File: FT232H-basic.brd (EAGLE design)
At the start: 57.1 x 25.4 mm, 26 parts, among them IC1 FT232H

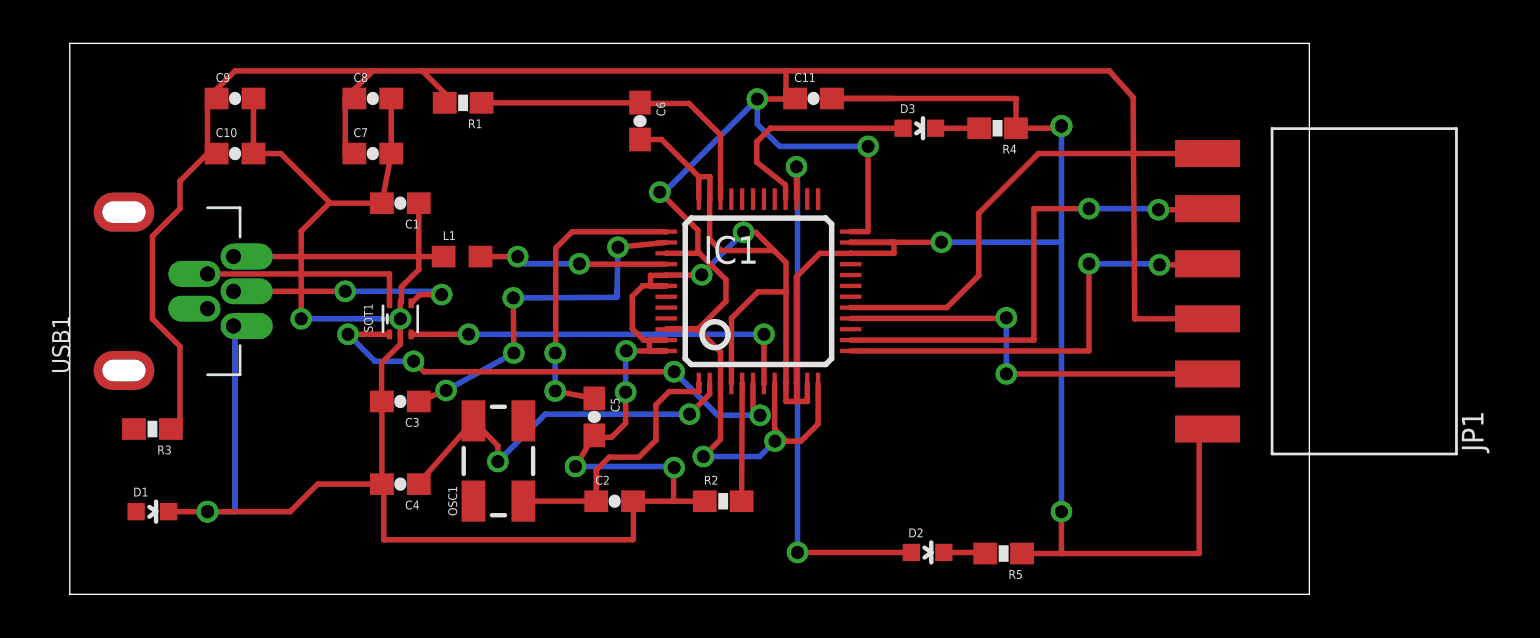
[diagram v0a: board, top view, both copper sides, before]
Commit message: routing improvements - much simpler, has bottom ground plane and top copper pour
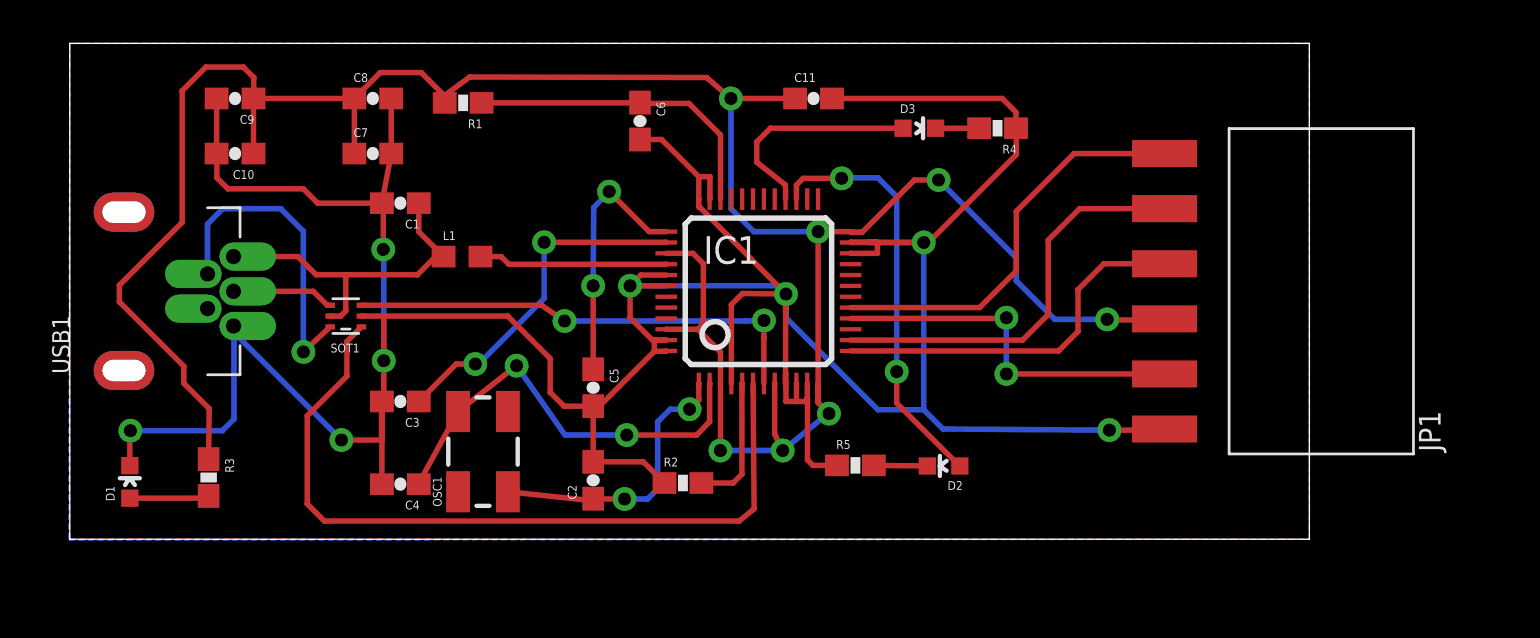
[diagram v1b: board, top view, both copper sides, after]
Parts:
- moved R5 7.95 mm to (36.2, 5.94), turned to 0 degrees
- moved D2 4.06 mm to (40.3, 5.92), turned to 90 degrees
- moved R3 3.42 mm to (6.40, 5.38), turned to 270 degrees
- moved SOT1 2.52 mm to (12.7, 12.8), turned to 90 degrees
- moved R2 2.03 mm to (28.3, 5.13)
- moved JP1 1.98 mm to (53.9, 14.0)
- moved D1 1.72 mm to (2.77, 5.18), turned to 0 degrees
- moved C2 1.38 mm to (24.1, 5.26), turned to 90 degrees
- moved C5 1.35 mm to (24.1, 9.53)
- moved OSC1 0.83 mm to (19.1, 6.58)
- turned C10 to 180 degrees
- turned C9 to 180 degrees
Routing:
- net GND: track 200.3 -> 178.4 mm, vias 12 -> 8
- net POWER: track 133.5 -> 118.5 mm, vias 5 -> 7
- net DM: track 24.1 -> 36.1 mm, vias 4 -> 0
- net N$6: track 11.2 -> 4.72 mm, vias 2 -> 0
- net RXLED: track 24.6 -> 19.4 mm
- net N$8: track 9.74 -> 14.7 mm, vias 0 -> 1
- net N$5: track 0.00 -> 3.67 mm
- net RXI: track 22.6 -> 19.0 mm, vias 2 -> 0
- net TXO: track 20.6 -> 17.3 mm, vias 2 -> 0
- net DP: track 18.5 -> 21.7 mm
- net N$7: track 17.7 -> 19.9 mm
- net N$1: track 13.9 -> 11.9 mm
- net CTS: track 19.1 -> 17.1 mm
- net DTR: track 20.7 -> 19.0 mm
- net OSC1: track 12.4 -> 13.6 mm, vias 0 -> 2
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- added copper zone on layer 16, net GND
- added copper zone on layer 1, net N$9
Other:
- board size 57.1 x 25.4 mm -> 57.1 x 22.9 mm

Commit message: board is slightly smaller now; traces in ground plane shorter
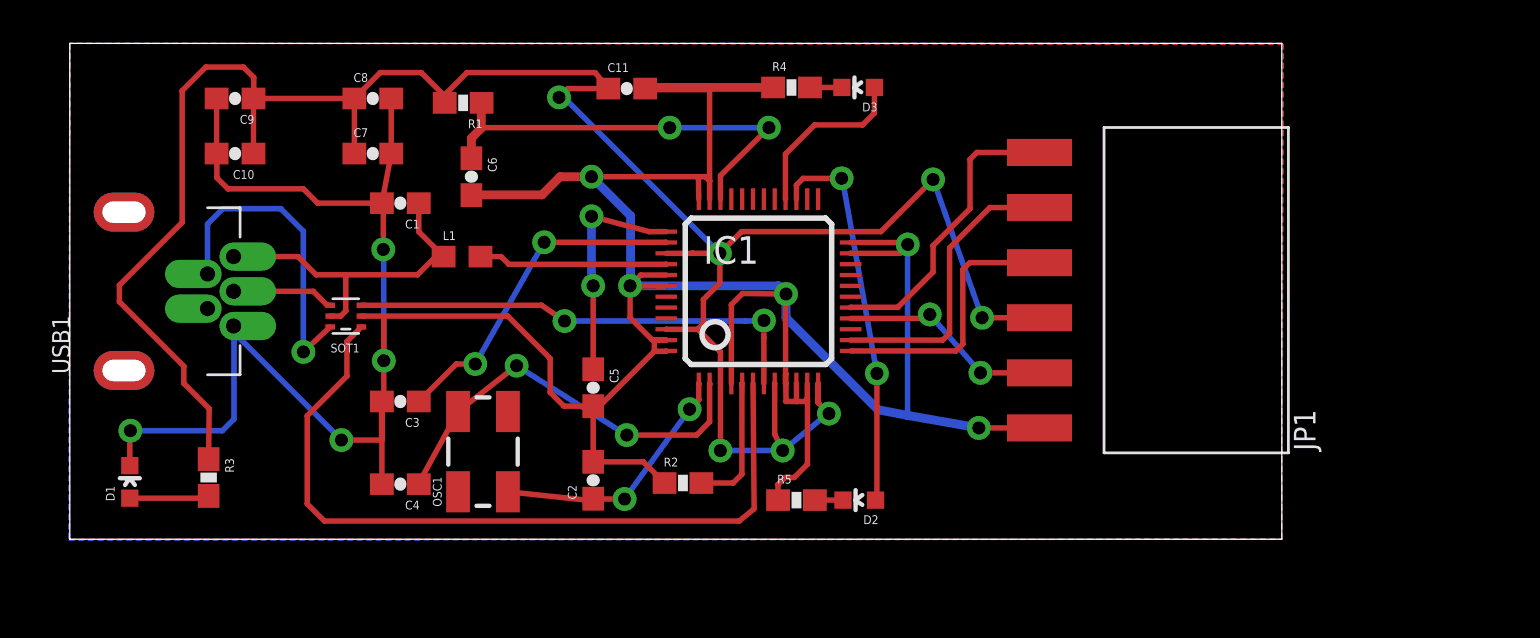
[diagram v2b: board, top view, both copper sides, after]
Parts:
- moved R4 9.68 mm to (33.3, 23.4), turned to 0 degrees
- moved C11 8.62 mm to (25.7, 23.3)
- moved C6 8.18 mm to (18.5, 19.3)
- moved JP1 5.77 mm to (48.1, 14.0)
- moved D2 4.19 mm to (36.4, 4.34)
- moved D3 3.39 mm to (36.3, 23.4), turned to 90 degrees
- moved R5 3.15 mm to (33.5, 4.34)
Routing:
- net POWER: track 118.5 -> 108.1 mm
- net CTS: track 17.1 -> 9.99 mm
- net N$3: track 14.6 -> 20.2 mm, vias 0 -> 2
- net RXI: track 19.0 -> 13.5 mm
- net DTR: track 19.0 -> 13.7 mm
- net TXO: track 17.3 -> 12.4 mm
- net GND: track 178.4 -> 173.8 mm, vias 8 -> 9
- net TXLED: track 10.3 -> 8.14 mm
- net RXLED: track 19.4 -> 17.9 mm
- net OSC1: track 13.6 -> 12.3 mm
- net N$1: track 11.9 -> 10.7 mm
- net N$11: track 2.46 -> 1.30 mm
- net N$7: track 19.9 -> 19.1 mm
- net N$10: track 2.01 -> 1.47 mm
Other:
- board size 57.1 x 22.9 mm -> 55.9 x 22.9 mm

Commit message: board is slightly smaller again, using space under TTL connector for traces
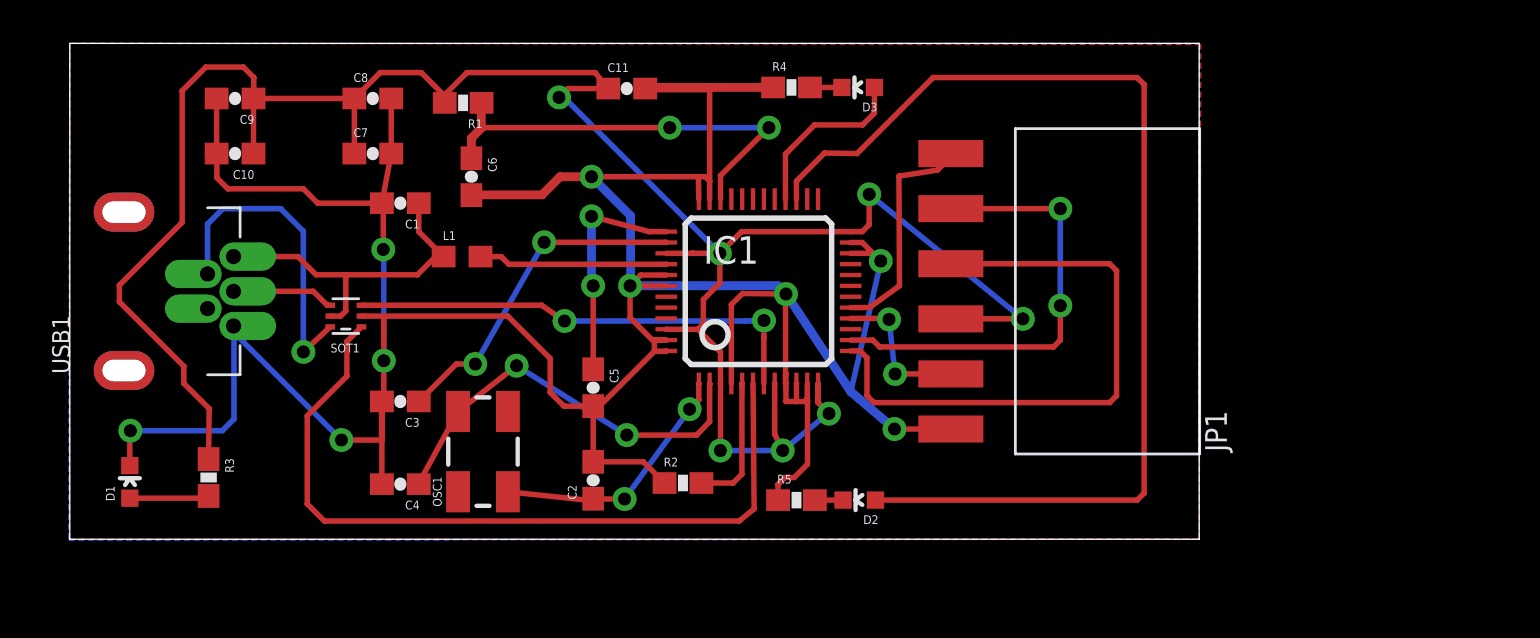
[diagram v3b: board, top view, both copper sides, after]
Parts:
- moved JP1 4.09 mm to (44.0, 14.0)
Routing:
- net RXLED: track 17.9 -> 50.3 mm, vias 2 -> 0
- net TXO: track 12.4 -> 27.9 mm
- net GND: track 173.8 -> 165.9 mm
- net RXI: track 13.5 -> 21.0 mm, vias 0 -> 2
- net DTR: track 13.7 -> 10.8 mm
- net CTS: track 9.99 -> 7.72 mm
- net POWER: track 108.1 -> 108.7 mm
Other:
- board size 55.9 x 22.9 mm -> 52.1 x 22.9 mm

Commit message: reduced board width
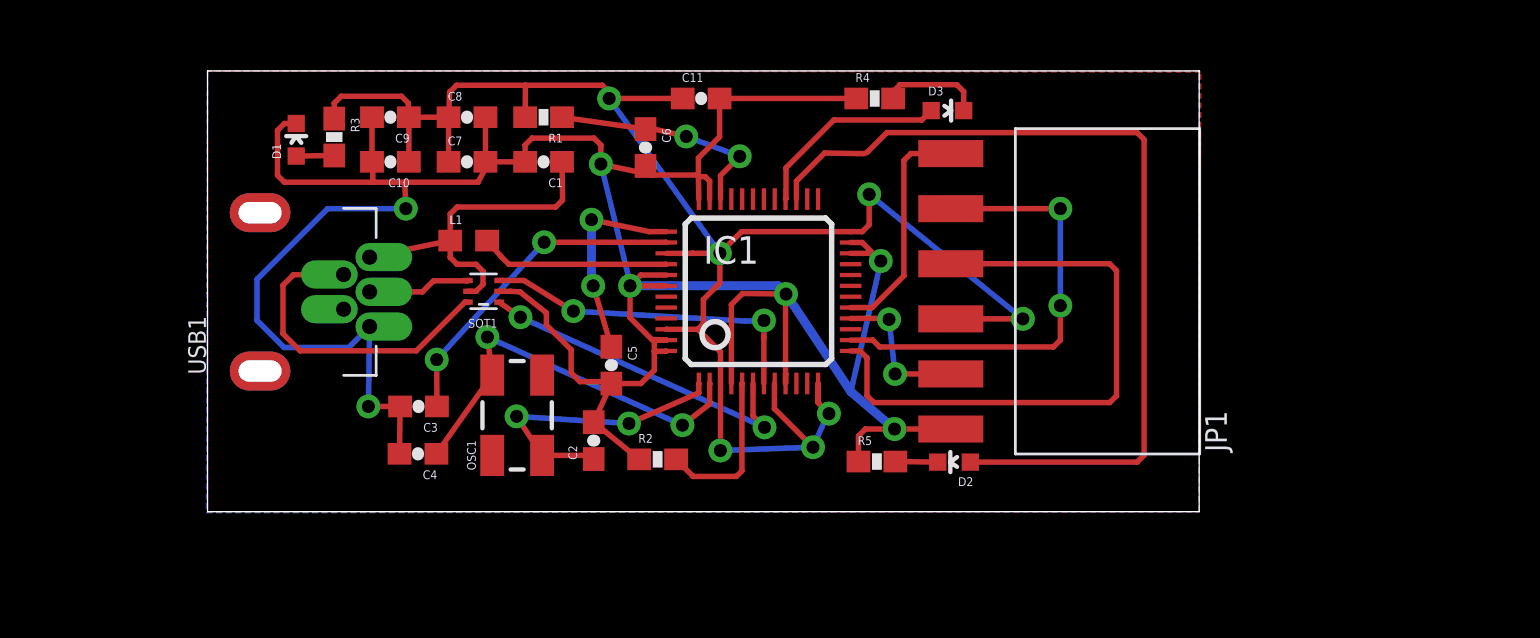
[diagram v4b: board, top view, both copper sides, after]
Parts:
- moved D1 17.5 mm to (10.4, 21.0)
- moved R3 16.7 mm to (12.2, 21.1)
- moved C6 8.14 mm to (26.5, 20.6)
- moved C9 7.21 mm to (14.8, 22.0)
- moved C10 7.17 mm to (14.8, 19.9)
- moved C1 6.87 mm to (21.8, 19.9)
- moved SOT1 6.45 mm to (19.1, 14.0)
- moved USB1 6.27 mm to (12.6, 13.9)
- moved D2 4.71 mm to (40.8, 6.10)
- moved C8 4.43 mm to (18.3, 22.0)
- moved C7 4.36 mm to (18.3, 19.9)
- moved D3 4.25 mm to (40.5, 22.3), turned to 270 degrees
- moved R5 4.11 mm to (37.2, 6.12)
- moved R4 3.87 mm to (37.1, 22.9)
- moved R1 3.77 mm to (21.8, 22.0)
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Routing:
- net POWER: track 108.7 -> 81.0 mm
- net GND: track 165.9 -> 140.8 mm, vias 9 -> 7
- net DM: track 36.1 -> 15.8 mm, vias 0 -> 2
- net RXLED: track 50.3 -> 40.6 mm
- net N$3: track 20.2 -> 10.8 mm
- net DP: track 21.7 -> 15.5 mm
- net N$10: track 1.47 -> 4.71 mm
- net N$5: track 3.67 -> 1.75 mm
- net OSC1: track 12.3 -> 13.7 mm
- net N$4: track 6.22 -> 7.50 mm
- net N$1: track 10.7 -> 9.56 mm
- net TXLED: track 8.14 -> 9.23 mm
- net N$11: track 1.30 -> 1.96 mm
- net N$8: track 14.7 -> 15.0 mm, vias 1 -> 0
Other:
- board size 52.1 x 22.9 mm -> 45.7 x 20.3 mm

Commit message: board routed, passes DRC, and has silkscreen; not all fonts are vector
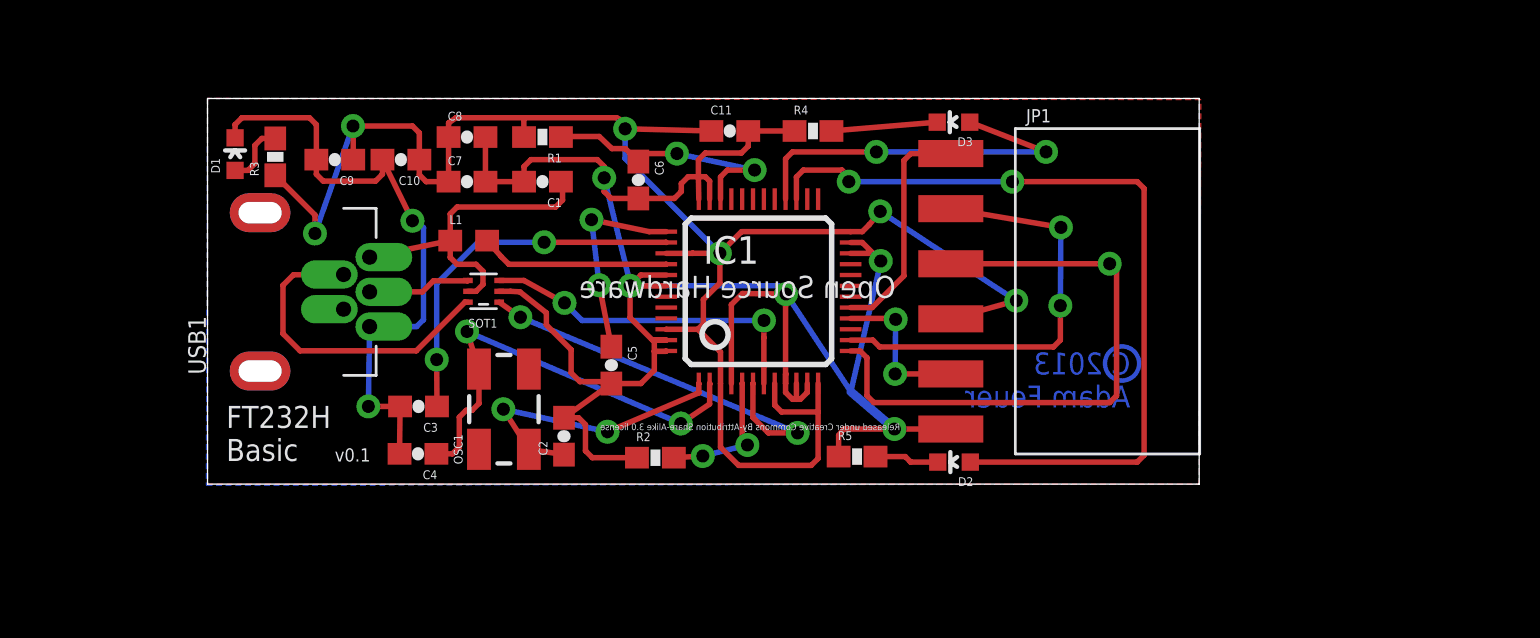
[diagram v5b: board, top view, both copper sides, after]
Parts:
- added U$1: (no value), SparkFun-Aesthetics:OSHW-LOGO-L
- added U$2: CC-BY-SA, creative-commons:CC-BY-SA
- moved C9 3.23 mm to (12.2, 20.0)
- moved R4 3.22 mm to (34.3, 21.4)
- moved D1 2.90 mm to (7.62, 20.3)
- moved R3 2.87 mm to (9.47, 20.2), turned to 90 degrees
- moved C11 2.00 mm to (30.4, 21.4)
- moved C6 1.53 mm to (26.2, 19.1)
- moved C2 1.39 mm to (22.8, 7.29)
- moved R5 0.94 mm to (36.3, 6.35)
- moved C1 0.92 mm to (21.8, 19.0)
- moved R1 0.92 mm to (21.8, 21.1)
- moved C7 0.91 mm to (18.3, 19.0)
- moved C8 0.91 mm to (18.3, 21.1)
- moved OSC1 0.67 mm to (20.0, 8.53)
- moved D3 0.60 mm to (40.7, 21.8), turned to 90 degrees
- moved C10 0.49 mm to (15.3, 20.0)
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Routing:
- net GND: track 140.8 -> 129.5 mm
- net TXLED: track 9.23 -> 17.8 mm, vias 0 -> 2
- net POWER: track 81.0 -> 84.7 mm, vias 7 -> 6
- net DM: track 15.8 -> 19.0 mm
- net RXLED: track 40.6 -> 38.1 mm, vias 0 -> 2
- net N$2: track 15.1 -> 17.0 mm
- net N$7: track 18.6 -> 20.4 mm
- net N$3: track 10.8 -> 12.4 mm
- net N$5: track 1.75 -> 2.96 mm
- net N$4: track 7.50 -> 6.39 mm, vias 0 -> 2
- net N$11: track 1.96 -> 2.98 mm
- net VUSB: track 16.2 -> 15.3 mm
- net RXI: track 21.0 -> 20.3 mm
- net TXO: vias 0 -> 1
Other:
- board size 45.7 x 20.3 mm -> 45.7 x 17.8 mm
- board text added: "5V"
- board text added: "BLK"
- board text added: "C 2013 Adam Feuer"
- board text added: "CTS"
- board text added: "DTR"
- board text added: "FT232H Basic"
- board text added: "GND"
- board text added: "GRN"
- board text added: "Open Source Hardware"
- board text added: "RX"
- board text added: "RXI"
- board text added: "Released under Creative Commons By-Attribution Share-Alike 3.0 license"
- board text added: "TX"
- board text added: "TXO"
- board text added: "v0.1"
